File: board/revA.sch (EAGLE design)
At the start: 58 parts, among them IC1 74HCT125, Q1 VND7NV04, Q2 VND7NV04, Q3 VND7NV04, Q4 VND7NV04

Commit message: Cleaning routing
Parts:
- IC1: device 74xx-eu:74ABT125PW -> misc:74ABT125PW
- LDO1: value LM2931 -> LM2931-5.0; device national-semiconductor:LM2936MM-3.3 -> national-semiconductor:LM2936M-5.0
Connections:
- net GND: now also LDO1.GND@1, LDO1.GND@2, LDO1.GND@3, LDO1.GND@4; no longer LDO1.GND

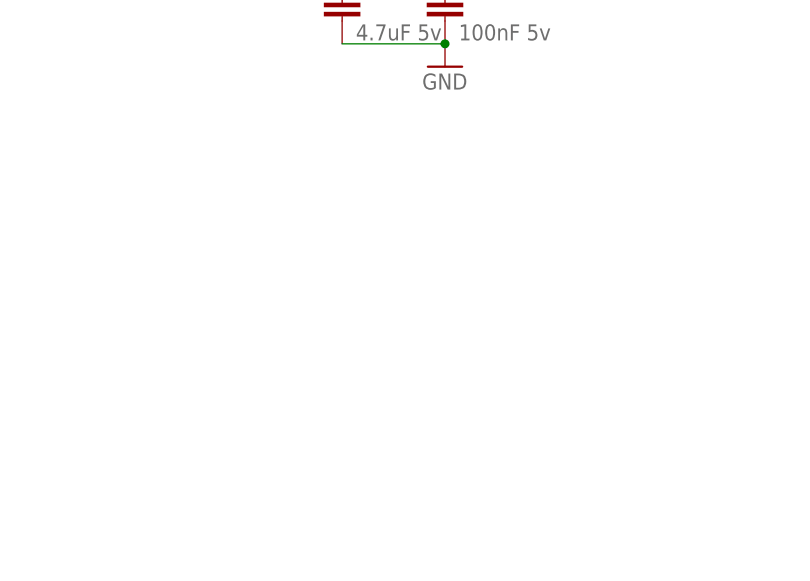
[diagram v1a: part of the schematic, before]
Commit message: Adding LED
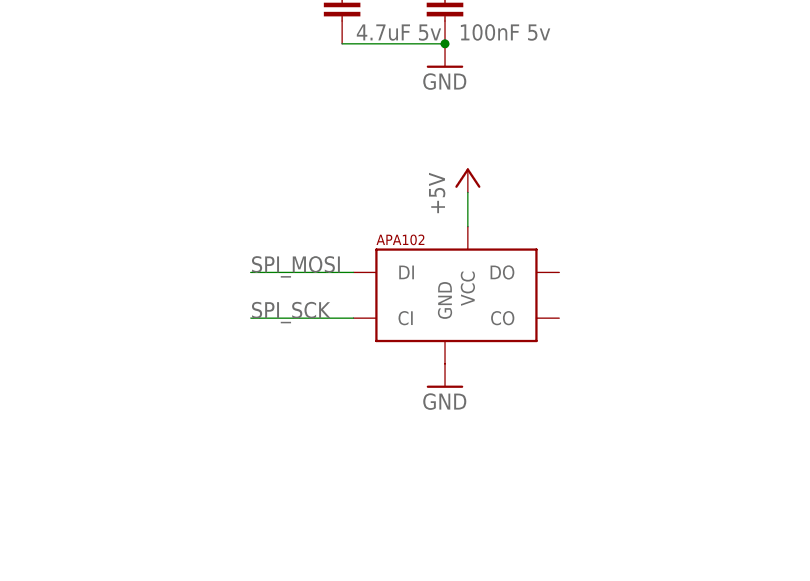
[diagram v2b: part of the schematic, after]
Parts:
- added LED: APA1025050, jos-ph:APA1025050
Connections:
- net +5V: now also LED.VCC
- net GND: now also LED.GND
- net SPI_MOSI: now also LED.DI
- net SPI_SCK: now also LED.CI
